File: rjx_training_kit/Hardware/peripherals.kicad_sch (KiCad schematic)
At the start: 73 parts, among them J4 LiPo_4.2V, J5 LiPo_4.2V, J6 CHG_OUT, J7 CAN_Bus, J8 CAN_Bus, Q2 BC817, Q3 BC817, Q4 BC808, Q5 BC817, SW2 SW_Push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

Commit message: [RJX]: New project structure
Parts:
- removed RV1: 10k, symbol Device:R_Potentiometer_US
- renumbered RV2 to RV1, SW2 to SW1
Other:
- note added: "JST-PH"
- note removed: "ADC1_IN5"
- note removed: "JST"
- note removed: "Potentiometer"
- moved on the sheet: D5, R31, R32, R33, SW1

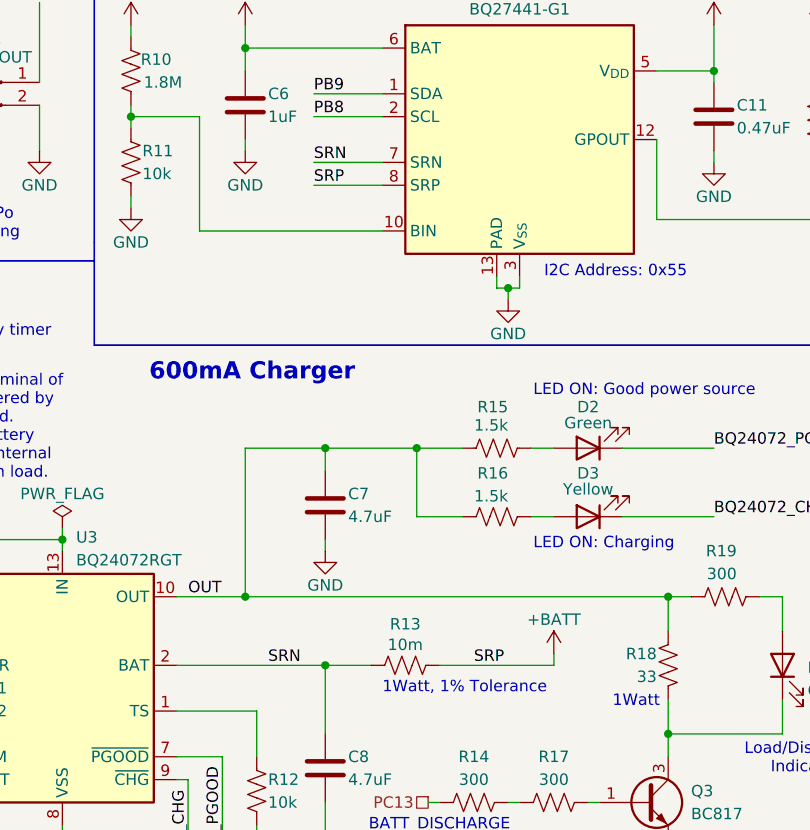
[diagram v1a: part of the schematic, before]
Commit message: [RJX]: Removed SRP label to eliminate annoying KiCad warning. This warning shows up because the SRP label is connected to +BATT.
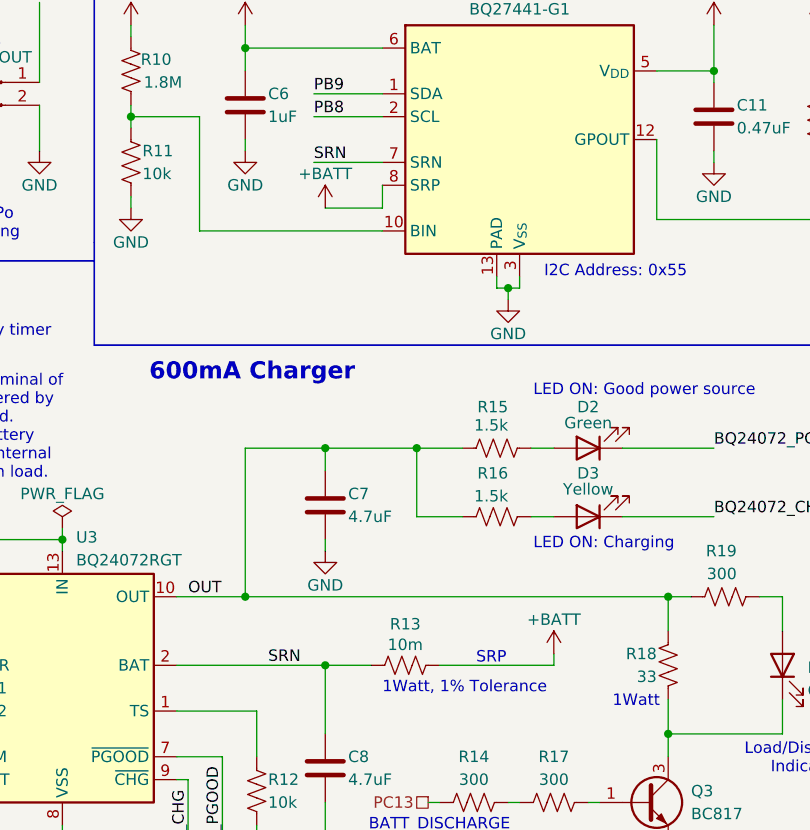
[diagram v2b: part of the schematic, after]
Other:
- note added: "SRP"
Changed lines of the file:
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@@
 		)
 	)
+	(text "SRP"
+		(exclude_from_sim no)
+		(at 99.314 100.838 0)
+		(effects
+			(font
+				(size 1.27 1.27)
+			)
+			(justify left)
+		)
+	)
 	(text "Load/Discharge \nIndicator"
 		(exclude_from_sim no)
@@
 	(wire
 		(pts
-			(xy 81.28 48.26) (xy 88.9 48.26)
+			(xy 82.55 50.8) (xy 88.9 50.8)
 		)
 		(stroke
@@
 	(wire
 		(pts
+			(xy 88.9 50.8) (xy 88.9 48.26)
+		)
+		(stroke
+			(width 0)
+			(type default)
+		)
+	)
+	(wire
+		(pts
 			(xy 147.32 72.39) (xy 170.18 72.39)
 		)
@@
 		)
 	)
-	(label "SRP"
-		(at 99.06 101.6 0)
-		(effects
-			(font
-				(size 1.27 1.27)
-			)
-			(justify left bottom)
-		)
-	)
 	(label "BQ24072_PGOOD"
 		(at 125.73 77.47 0)
@@
 		)
 	)
-	(label "SRP"
-		(at 81.28 48.26 0)
-		(effects
-			(font
-				(size 1.27 1.27)
-			)
-			(justify left bottom)
-		)
-	)
 	(label "TMR"
 		(at 35.56 101.6 0)
@@
 					(unit 1)
 				)
+			)
+		)
+	)
+	(symbol
+		(lib_id "power:+BATT")
+		(at 82.55 50.8 0)
+		(unit 1)
+		(exclude_from_sim no)
+		(in_bom yes)
+		(on_board yes)
+		(dnp no)
+		(property "Reference" "#PWR086"
+			(at 82.55 54.61 0)
+			(effects
+				(font
+					(size 1.27 1.27)
+				)
+				(hide yes)
+			)
+		)
+		(property "Value" "+BATT"
+			(at 82.55 46.99 0)
+			(effects
+				(font
+					(size 1.27 1.27)
+				)
+			)
+		)
+		(property "Footprint" ""
+			(at 82.55 50.8 0)
+			(effects
+				(font
+					(size 1.27 1.27)
+				)
+				(hide yes)
+			)
+		)
+		(property "Datasheet" ""
+			(at 82.55 50.8 0)
+			(effects
+				(font
+					(size 1.27 1.27)
+				)
+				(hide yes)
+			)
+		)
+		(property "Description" "Power symbol creates a global label with name \"+BATT\""
+			(at 82.55 50.8 0)
+			(effects
+				(font
+					(size 1.27 1.27)
+				)
+				(hide yes)
+			)
+		)
+		(pin "1"
+		)
+		(instances
+			(project "rjx_training_kit"
+				(path "/c10d0f5f-1570-4ced-80f8-bf69ea514c66/84fb618b-c7c4-4945-a2e1-bdfcc1b3a7be"
+					(reference "#PWR086")
+					(unit 1)
+				)
